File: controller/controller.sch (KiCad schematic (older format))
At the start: 8 parts, among them J1 Screw_Terminal_01x02, J2 Screw_Terminal_01x04, J3 Screw_Terminal_01x03, J4 Screw_Terminal_01x04, U1 WeMos_D1_mini, U2 NodeMCU_ESP12E

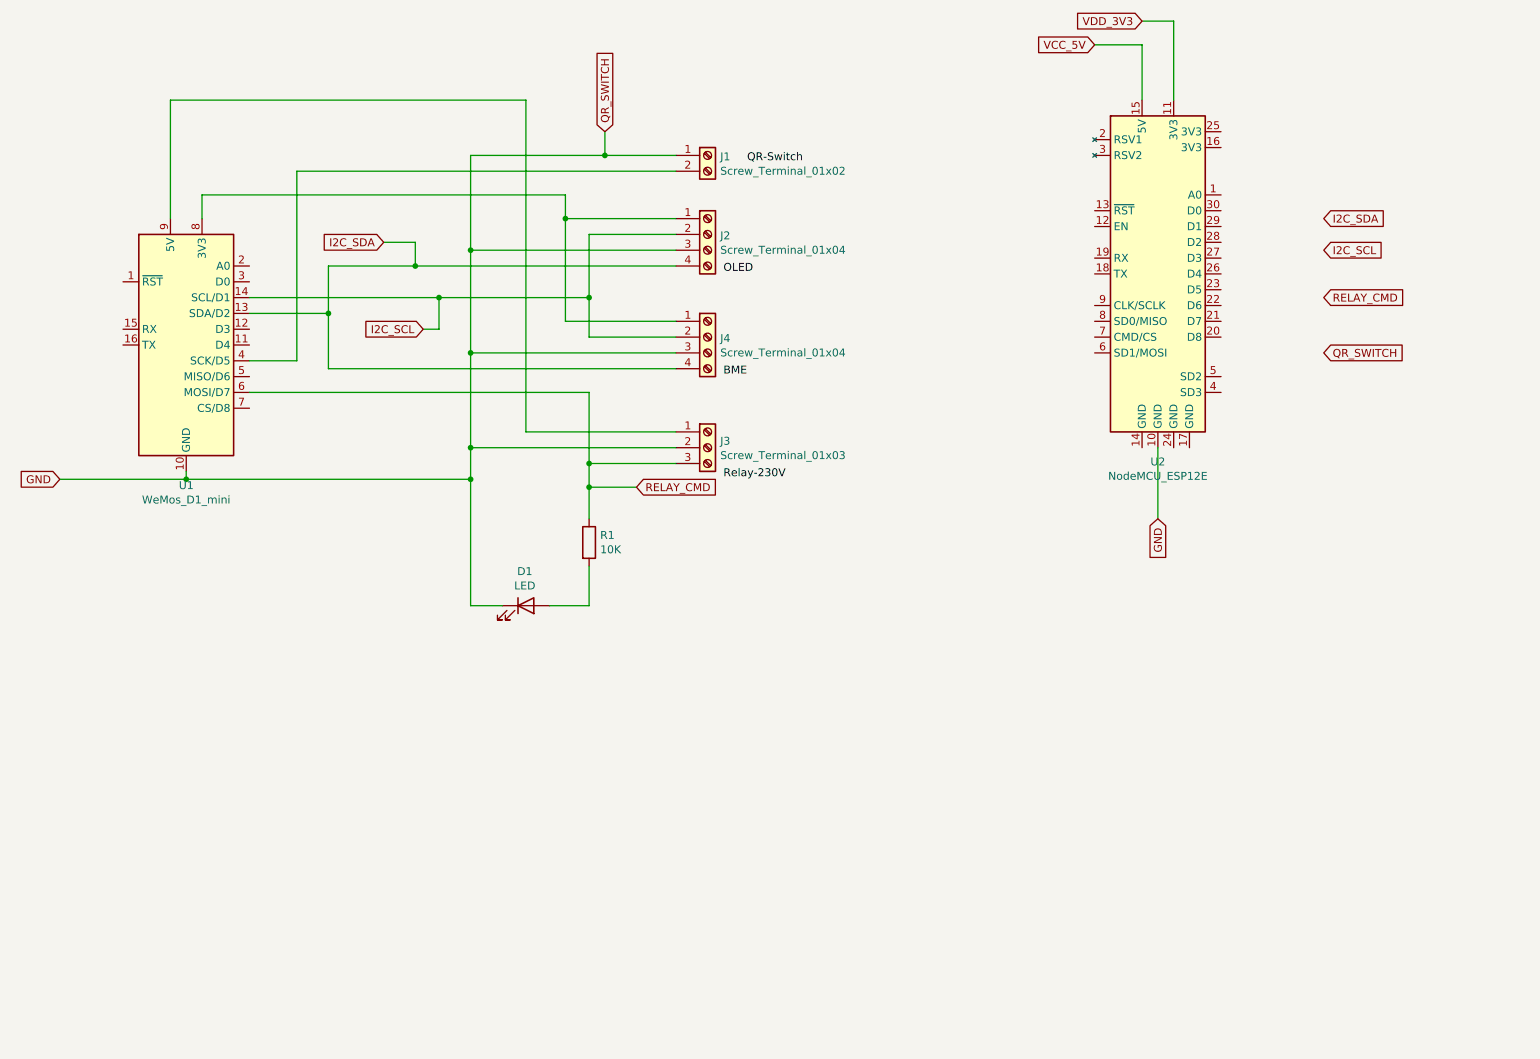
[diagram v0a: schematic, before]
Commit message: Released to production V0.2
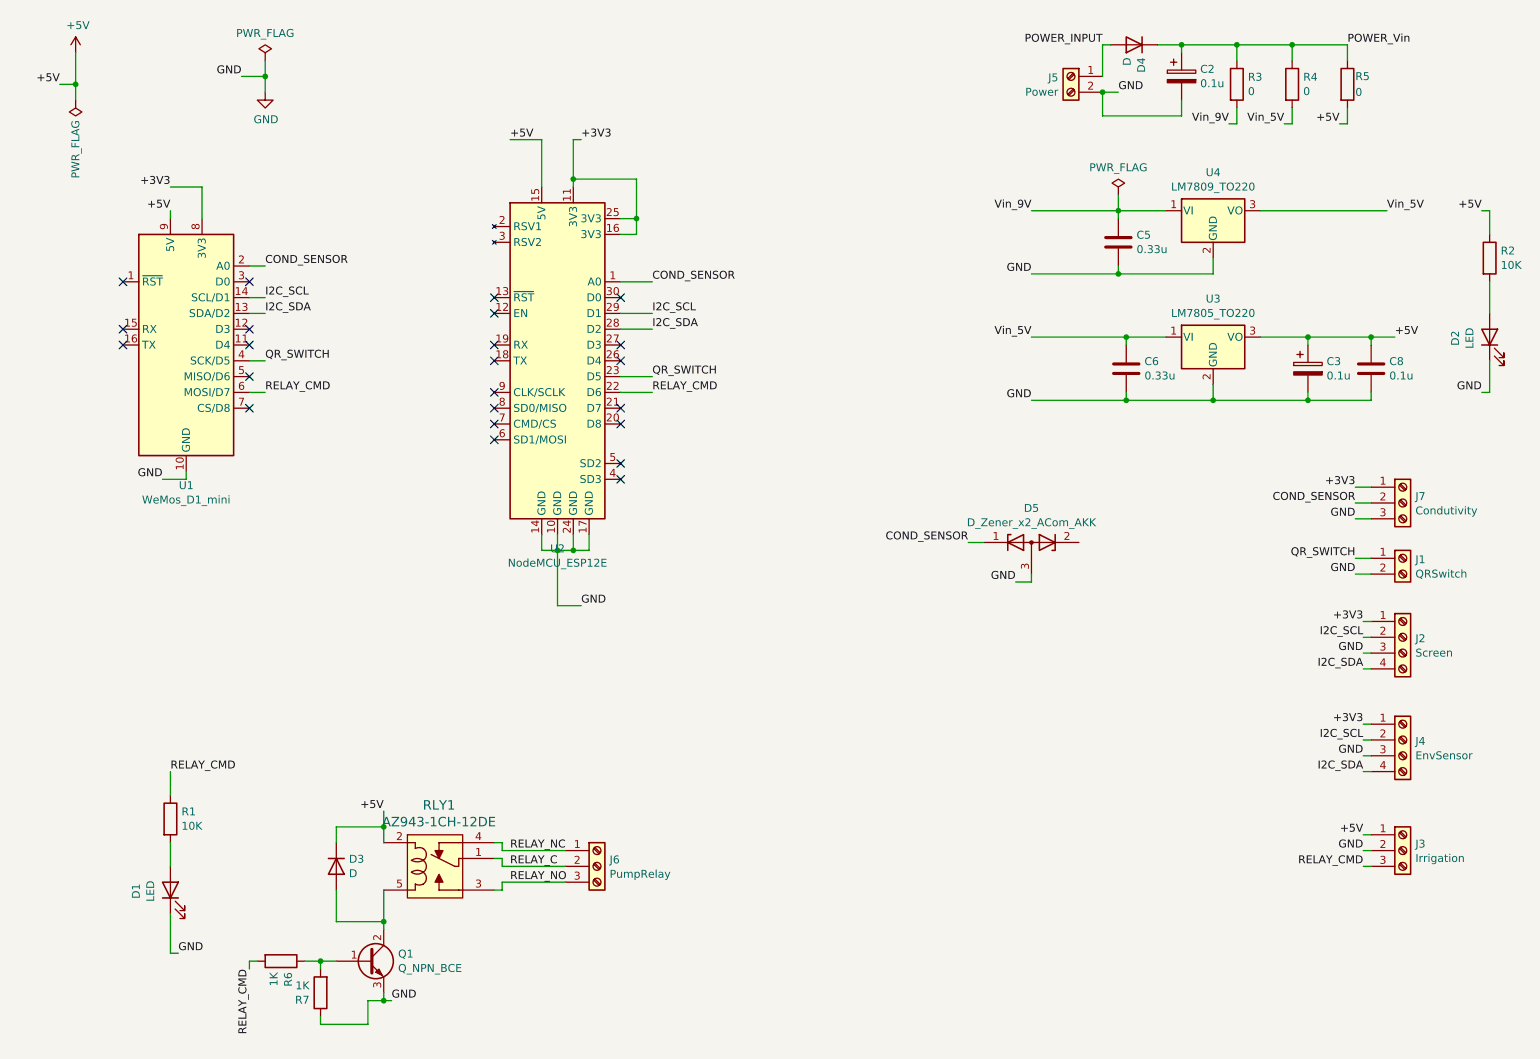
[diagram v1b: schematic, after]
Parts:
- added C2, C3: 0.1u, Capacitor_THT:CP_Radial_D5.0mm_P2.00mm, symbol Device:CP
- added C5, C6: 0.33u, Capacitor_SMD:C_0805_2012Metric, symbol Device:C
- added C8: 0.1u, Capacitor_SMD:C_0805_2012Metric, symbol Device:C
- added D2: LED, LED_THT:LED_D3.0mm, symbol Device:LED
- added D3, D4: D, Diode_THT:D_DO-41_SOD81_P7.62mm_Horizontal, symbol Device:D
- added D5: D_Zener_x2_ACom_AKK, Package_TO_SOT_SMD:SOT-23, symbol Device:D_Zener_x2_ACom_KKA
- added J5: Power, TerminalBlock:TerminalBlock_bornier-2_P5.08mm, symbol Connector:Screw_Terminal_01x02
- added J6: PumpRelay, TerminalBlock:TerminalBlock_bornier-3_P5.08mm, symbol Connector:Screw_Terminal_01x03
- added J7: Condutivity, TerminalBlock:TerminalBlock_bornier-3_P5.08mm, symbol Connector:Screw_Terminal_01x03
- added Q1: Q_NPN_BCE, Package_TO_SOT_THT:TO-92, symbol Device:Q_NPN_BCE
- added R2: 10K, Resistor_SMD:R_0805_2012Metric, symbol Device:R
- added R3, R4, R5: 0, Resistor_SMD:R_0805_2012Metric, symbol Device:R
- added R6, R7: 1K, Resistor_SMD:R_0805_2012Metric, symbol Device:R
- added RLY1: AZ943-1CH-12DE, LCP_Footprints:Relay_SPDT_ZETTLER_AZ943_Series_Form_C, symbol dk_Automotive-Relays:JSM1-12V-5
- added U3: LM7805_TO220, Package_TO_SOT_THT:TO-220-3_Vertical, symbol Regulator_Linear:LM7805_TO220
- added U4: LM7809_TO220, Package_TO_SOT_THT:TO-220-3_Vertical, symbol Regulator_Linear:LM7809_TO220
- J1: value Screw_Terminal_01x02 -> QRSwitch; footprint (none) -> TerminalBlock:TerminalBlock_bornier-2_P5.08mm
- J2: value Screw_Terminal_01x04 -> Screen; footprint (none) -> TerminalBlock:TerminalBlock_bornier-4_P5.08mm
- J3: value Screw_Terminal_01x03 -> Irrigation; footprint (none) -> TerminalBlock:TerminalBlock_bornier-3_P5.08mm
- J4: value Screw_Terminal_01x04 -> EnvSensor; footprint (none) -> TerminalBlock:TerminalBlock_bornier-4_P5.08mm
- R1: footprint Resistor_THT:R_Axial_DIN0204_L3.6mm_D1.6mm_P1.90mm_Vertical -> Resistor_SMD:R_0805_2012Metric
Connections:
- net VCC_5V is gone; now on net +5V: U2.15 (5V)
- net VDD_3V3 is gone; now on net +3V3: U2.11 (3V3)
- net GND: now also J1.2 (Pin_2), U2.14 (GND), U2.17 (GND), U2.24 (GND), C2.2, C3.2, C5.2, C6.2, C8.2, D2.1 (K), D5.3 (A), J5.2 (Pin_2), J7.3 (Pin_3), Q1.3 (E), R7.1, U3.2 (GND), U4.2 (GND); no longer J1.1 (Pin_1)
- net I2C_SCL: now also U2.29 (D1)
- net I2C_SDA: now also U2.28 (D2)
- net RELAY_CMD: now also U2.22 (D6), R6.2
- net COND_SENSOR: now reaches U1.2 (A0)
- net COND_SENSOR: now also U2.1 (A0), D5.1 (K), J7.2 (Pin_2)
- net QR_SWITCH: now reaches U1.4 (SCK/D5)
- net QR_SWITCH: now also J1.1 (Pin_1), U2.23 (D5); no longer J1.2 (Pin_2)
- net +3V3: now reaches J2.1 (Pin_1), J4.1 (Pin_1), U1.8 (3V3)
- net +3V3: now also U2.16 (3V3), U2.25 (3V3), J7.1 (Pin_1)
- net +5V: now reaches J3.1 (Pin_1), U1.9 (5V)
- net +5V: now also C3.1, C8.1, D3.1 (K), R2.1, R5.2, RLY1.2, U3.3 (VO)
- new net: D2.2 (A), R2.2
- new net: Q1.1 (B), R6.1, R7.2
- new net: D3.2 (A), Q1.2 (C), RLY1.5
- new net POWER_INPUT: D4.2 (A), J5.1 (Pin_1)
- new net POWER_Vin: C2.1, D4.1 (K), R3.1, R4.1, R5.1
- new net RELAY_C: J6.2 (Pin_2), RLY1.1 (COM)
- new net RELAY_NC: J6.1 (Pin_1), RLY1.4 (NC)
- new net RELAY_NO: J6.3 (Pin_3), RLY1.3 (NO)
- new net Vin_5V: C6.1, R4.2, U3.1 (VI), U4.3 (VO)
- new net Vin_9V: C5.1, R3.2, U4.1 (VI)
- no-connect marks 0 -> 23
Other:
- moved on the sheet: D1, J1, J2, J3, J4, R1, U2

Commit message: Production version. First iteration for correction
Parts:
- U2: symbol LCP_MCU_Module:NodeMCU_ESP12E -> controller-rescue:NodeMCU_ESP12E-LCP_MCU_Module
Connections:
- net +3V3: now also U2.21 (3V3), U2.30 (3V3); no longer U2.16 (3V3), U2.25 (3V3)
- net GND: now also U2.22 (GND), U2.29 (GND); no longer U2.17 (GND), U2.24 (GND)
- net I2C_SCL: now also U2.17 (D1); no longer U2.29 (D1)
- net I2C_SDA: now also U2.18 (D2); no longer U2.28 (D2)
- net RELAY_CMD: now also U2.24 (D6); no longer U2.22 (D6)
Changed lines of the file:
@@
 	10100 4000 10000 4000
 $Comp
-L LCP_MCU_Module:NodeMCU_ESP12E U2
+L controller-rescue:NodeMCU_ESP12E-LCP_MCU_Module U2
 U 1 1 60ABC8B2
 P 4950 2750
